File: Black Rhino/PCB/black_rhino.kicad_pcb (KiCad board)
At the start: 2 copper layers, 271.5 x 118.3 mm, 175 parts, among them SW1 SW_Push, U1 ATmega32U4-AU, Y1 16MHz

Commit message: Improve Black Rhino-PCB
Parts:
- moved C2 0.28 mm to (164.3, 48.0)
- moved C1 0.28 mm to (164.3, 57.6)
- moved Y1 0.28 mm to (164.3, 52.8)
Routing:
- net Net-(R1-Pad2): track 75.0 -> 74.4 mm

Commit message: Rewire Black Rhino-PCB
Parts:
- removed D68: LED, LED_SMD:LED_0805_2012Metric
- removed H1, H10, H11, H12, H13, H14, H15, H16, H17, H18, H19, H2, H20, H21, H22, H23, H3, H4, H5, H6, H7, H8, H9: MountingHole, MountingHole:MountingHole_2mm
- removed R5: 470, Resistor_SMD:R_0805_2012Metric
- moved C7 108.4 mm to (126.4, 156.7), turned to 0 degrees
- moved R2 106.7 mm to (272.9, 92.3), turned to 90 degrees
- moved R1 105.6 mm to (121.2, 145.2), turned to 90 degrees
- moved R3 105.4 mm to (270.5, 92.3), turned to 90 degrees
- moved F1 105.1 mm to (268.0, 92.8), turned to 90 degrees
- moved C3 104.3 mm to (120.4, 148.5)
- moved C4 103.6 mm to (118.6, 145.2), turned to 270 degrees
- moved C6 98.3 mm to (132.5, 156.7)
- moved U1 96.5 mm to (129.4, 148.4), turned to 0 degrees
- moved USB1 95.0 mm to (272.1, 83.5), turned to 270 degrees
- moved C2 94.2 mm to (126.2, 134.2), turned to 90 degrees
- moved R4 91.3 mm to (138.4, 153.2), turned to 180 degrees
- moved SW1 89.2 mm to (272.3, 118.3), turned to 0 degrees
- moved Y1 88.3 mm to (130.0, 134.2), turned to 180 degrees
- moved C5 86.2 mm to (138.4, 144.4), turned to 0 degrees
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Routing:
- net Net-(R2-Pad1): track 28.9 -> 217.7 mm
- net Net-(R3-Pad1): track 29.5 -> 216.7 mm
- net ROW3: track 458.0 -> 274.7 mm, vias 0 -> 15
- net ROW2: track 445.5 -> 272.3 mm, vias 0 -> 16
- net GND: track 197.0 -> 26.5 mm, vias 3 -> 435
- net ROW4: track 477.0 -> 307.9 mm, vias 0 -> 13
- net +5V: track 94.8 -> 242.8 mm, vias 4 -> 2
- net ROW1: track 435.5 -> 318.7 mm, vias 0 -> 16
- net Net-(R1-Pad2): track 74.4 -> 175.7 mm
- net ROW0: track 397.1 -> 330.9 mm, vias 0 -> 17
- net COL9: track 125.8 -> 63.8 mm, vias 0 -> 1
- net LED0: track 53.7 -> 0.00 mm, vias 2 -> 0
- net COL13: track 204.0 -> 237.4 mm, vias 0 -> 1
- net COL7: track 70.2 -> 102.4 mm, vias 0 -> 2
- net COL12: track 180.9 -> 206.4 mm, vias 0 -> 1
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- removed copper zone on F.Cu, net +5V
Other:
- board size 271.5 x 118.3 mm -> 271.5 x 109.5 mm
- board text removed: "+5V"
- board text removed: "Diceros Bicornis"
- board text removed: "GND"

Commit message: Improve Black Rhino-PCB
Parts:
- added D68: LED, LED_SMD:LED_0805_2012Metric, F.Cu at (196.1, 58.7)
- added H1: MountingHole, MountingHole:MountingHole_2mm, B.Cu at (16.7, 59.5)
- added H10: MountingHole, MountingHole:MountingHole_2mm, B.Cu at (148.4, 129.4)
- added H11: MountingHole, MountingHole:MountingHole_2mm, B.Cu at (91.3, 148.4)
- added H12: MountingHole, MountingHole:MountingHole_2mm, B.Cu at (167.5, 148.4)
- added H2: MountingHole, MountingHole:MountingHole_2mm, B.Cu at (280.2, 59.5)
- added H3: MountingHole, MountingHole:MountingHole_2mm, B.Cu at (16.7, 161.1)
- added H4: MountingHole, MountingHole:MountingHole_2mm, B.Cu at (280.2, 161.1)
- added H5: MountingHole, MountingHole:MountingHole_2mm, B.Cu at (53.2, 91.3)
- added H6: MountingHole, MountingHole:MountingHole_2mm, B.Cu at (243.7, 91.3)
- added H7: MountingHole, MountingHole:MountingHole_2mm, B.Cu at (53.2, 129.4)
- added H8: MountingHole, MountingHole:MountingHole_2mm, B.Cu at (243.7, 129.4)
- added H9: MountingHole, MountingHole:MountingHole_2mm, B.Cu at (148.4, 91.3)
- added R5: 470, Resistor_SMD:R_0805_2012Metric, B.Cu at (128.1, 61.8)
- moved F1 28.4 mm to (258.7, 66.0)
- moved R2 28.4 mm to (263.6, 65.5)
- moved R3 28.3 mm to (261.4, 65.5)
- moved USB1 27.8 mm to (262.9, 57.3)
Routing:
- net LED0: track 0.00 -> 100.1 mm, vias 0 -> 2
- net COL9: track 63.8 -> 141.6 mm
- net Net-(D68-Pad2): track 0.00 -> 69.1 mm, vias 0 -> 1
- net Net-(R2-Pad1): track 217.7 -> 239.7 mm
- net +5V: track 242.8 -> 263.4 mm
- net Net-(R3-Pad1): track 216.7 -> 235.5 mm
- net VCC: track 5.17 -> 0.00 mm
- net ROW1: track 318.7 -> 320.0 mm, vias 16 -> 17
- net ROW3: track 274.7 -> 273.8 mm
- net GND: track 26.5 -> 27.2 mm, vias 435 -> 447
- net D-: track 3.62 -> 3.05 mm

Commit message: Improve Black Rhino-PCB
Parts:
- moved H12 38.1 mm to (205.6, 148.4)
- moved R5 15.1 mm to (128.1, 77.0)
- moved SW1 0.79 mm to (272.3, 117.5)
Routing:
- net Net-(D68-Pad2): track 69.1 -> 84.3 mm
- net LED0: track 100.1 -> 85.0 mm
- net VCC: track 0.00 -> 4.29 mm
- net COL13: track 236.9 -> 241.1 mm
- net GND: track 27.2 -> 28.5 mm, vias 447 -> 395
- net COL11: track 185.0 -> 186.2 mm
- net COL10: track 164.9 -> 166.1 mm
- net (no net): vias 0 -> 2

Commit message: Improve Black Rhino-PCB
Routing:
- net GND: track 28.5 -> 29.9 mm, vias 395 -> 417
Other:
- rule pad_to_mask_clearance: 0.051 -> 0.05
- rule solder_mask_min_width: 0.25 -> 0.254
- rule trace_min: 0.2 -> 0.127
- rule via_min_drill: 0.3 -> 0.2
- rule via_min_size: 0.4 -> 0.45

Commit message: Improve Black Rhino-PCB
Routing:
- net COL13: track 241.1 -> 232.0 mm
- net GND: track 29.9 -> 32.8 mm, vias 417 -> 418
- net +5V: track 263.4 -> 264.1 mm
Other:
- board text added: "Diceros Bicornis"
- board text added: "PCB made by KingMalur."

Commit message: Improve Black Rhino-PCB
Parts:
- moved R4 1.27 mm to (139.7, 153.2)
- moved C6 1.24 mm to (132.5, 158.0), turned to 270 degrees
- moved C7 1.09 mm to (126.4, 157.8), turned to 270 degrees
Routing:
- net Net-(R2-Pad1): track 240.2 -> 244.0 mm
- net VCC: track 4.29 -> 6.15 mm
- net +5V: track 264.1 -> 265.9 mm
- net COL6: track 94.8 -> 96.2 mm
- net Net-(R4-Pad2): track 3.02 -> 4.46 mm
- net Net-(R3-Pad1): track 235.6 -> 236.3 mm
- net ROW4: track 307.9 -> 308.4 mm
- net GND: vias 418 -> 421

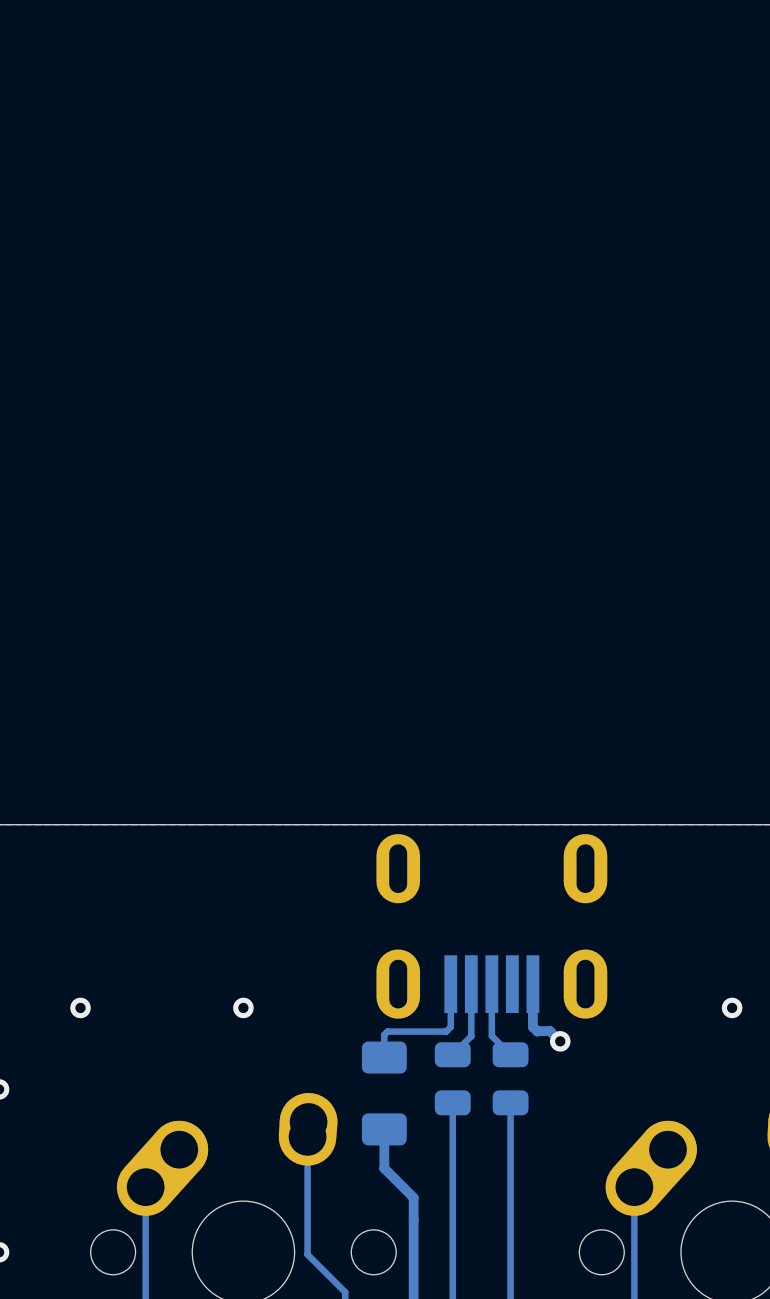
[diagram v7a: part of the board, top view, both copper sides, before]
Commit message: Add USB-C to Black Rhino
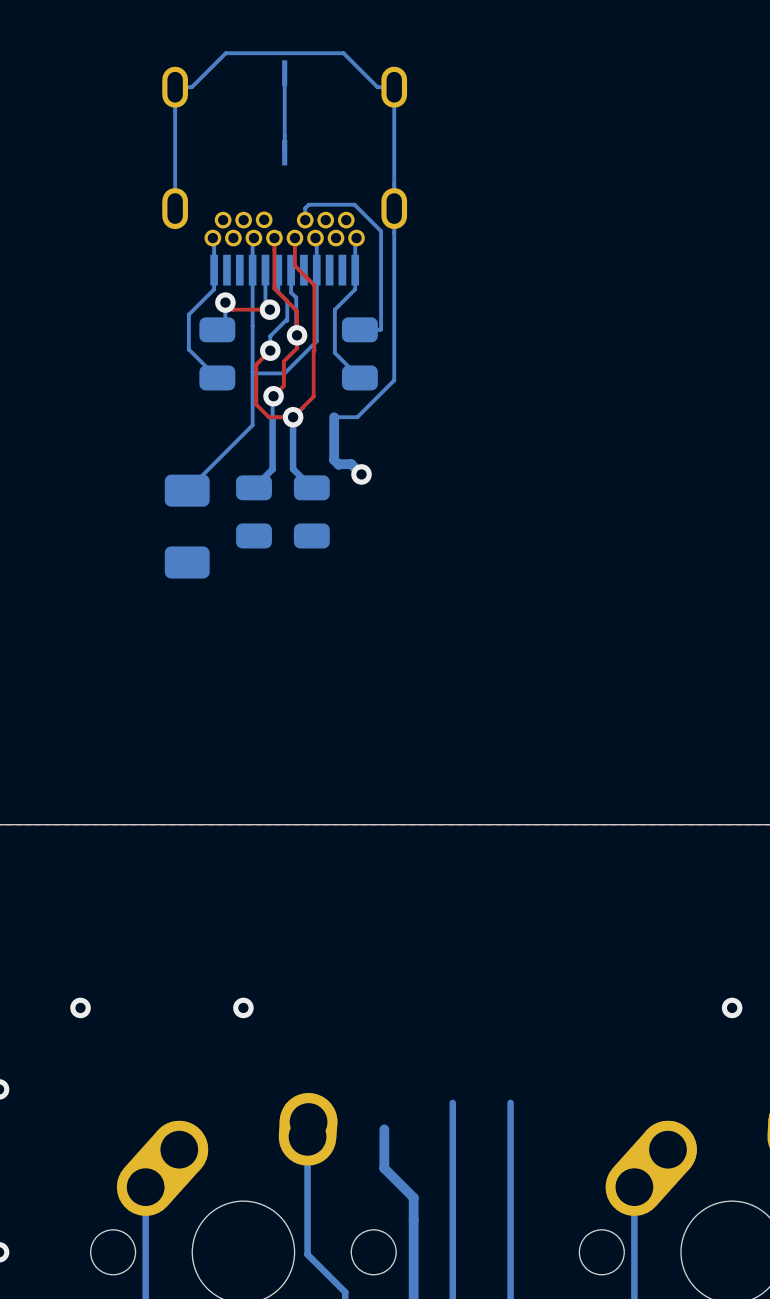
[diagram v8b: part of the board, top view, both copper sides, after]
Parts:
- removed F1: 500mA, Fuse:Fuse_1206_3216Metric
- removed USB1: Molex-0548190589, random-keyboard-parts:Molex-0548190589
- added F2: 500mA, Fuse:Fuse_1206_3216Metric, B.Cu at (251.0, 43.9)
- added R6: 5k1, Resistor_SMD:R_0805_2012Metric, B.Cu at (257.7, 37.2)
- added R7: 5k1, Resistor_SMD:R_0805_2012Metric, B.Cu at (252.2, 37.2)
- added USB2: Wurth-632723300011, Type-C:Wurth-632723300011, B.Cu at (254.8, 23.4)
- moved R2 23.4 mm to (255.9, 43.4)
- moved R3 23.4 mm to (253.6, 43.4)
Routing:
- net Net-(USB2-Pad26): track 0.00 -> 31.7 mm, vias 0 -> 1
- net D+: track 3.23 -> 19.1 mm, vias 0 -> 2
- net VCC: track 6.15 -> 18.0 mm
- net D-: track 3.05 -> 13.7 mm, vias 0 -> 2
- net GND: track 32.8 -> 42.3 mm, vias 421 -> 420
- net Net-(R6-Pad1): track 0.00 -> 8.56 mm
- net Net-(R7-Pad1): track 0.00 -> 4.66 mm, vias 0 -> 2
- net Net-(USB2-Pad27): track 0.00 -> 3.10 mm
